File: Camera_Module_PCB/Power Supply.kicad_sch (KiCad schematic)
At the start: 18 parts

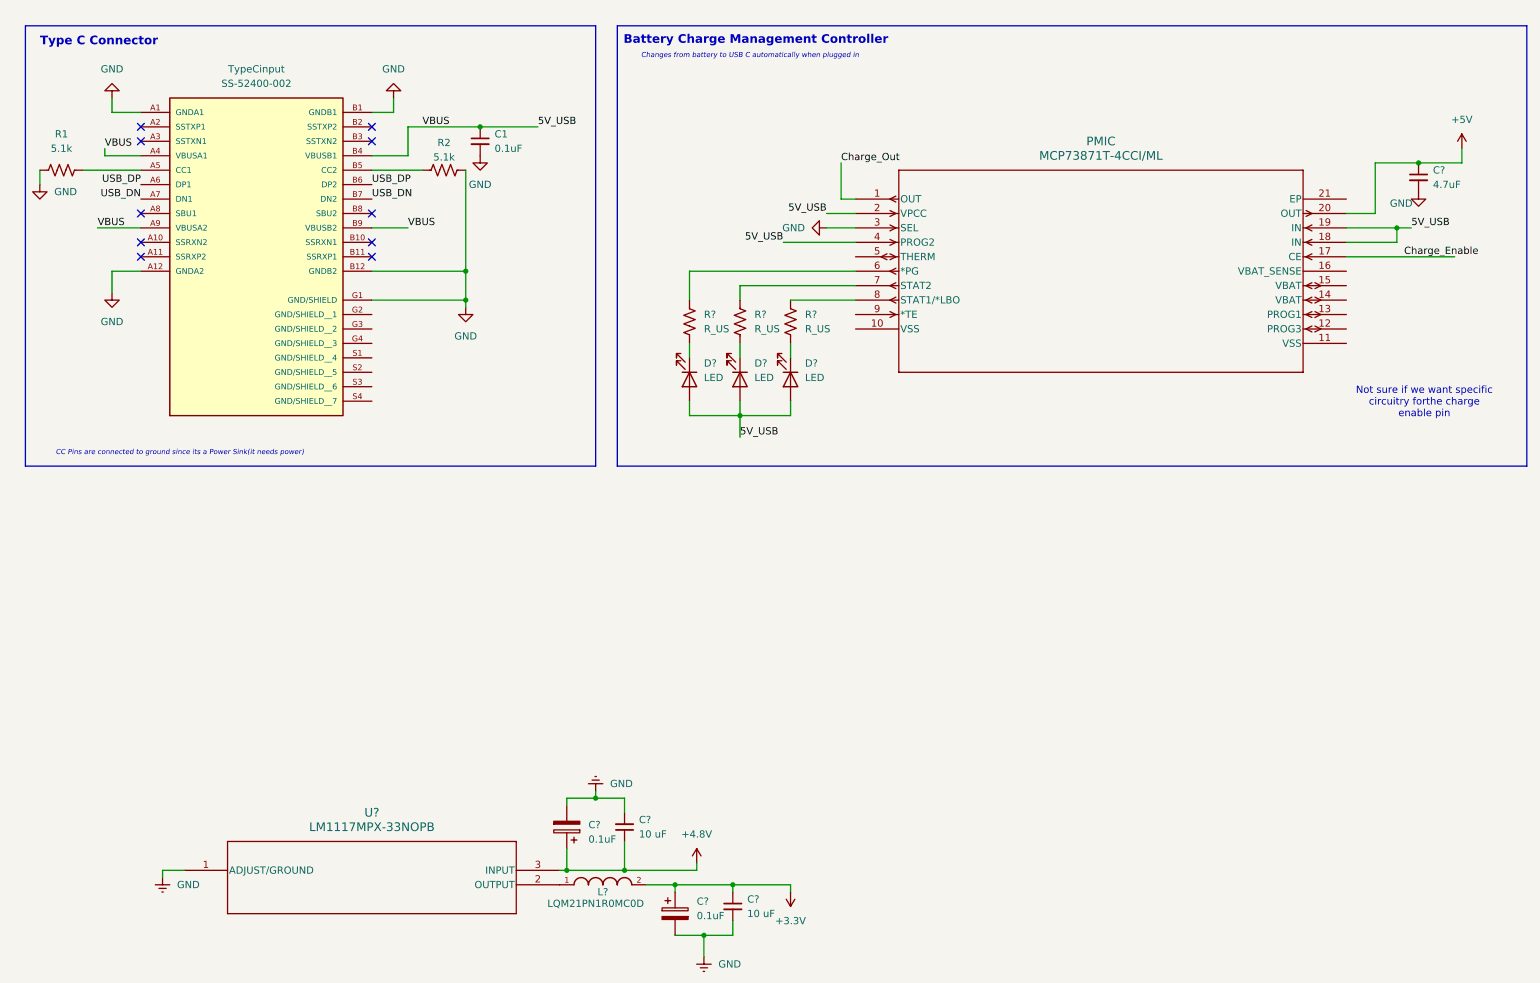
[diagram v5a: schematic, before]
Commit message: Small Additions to Charger
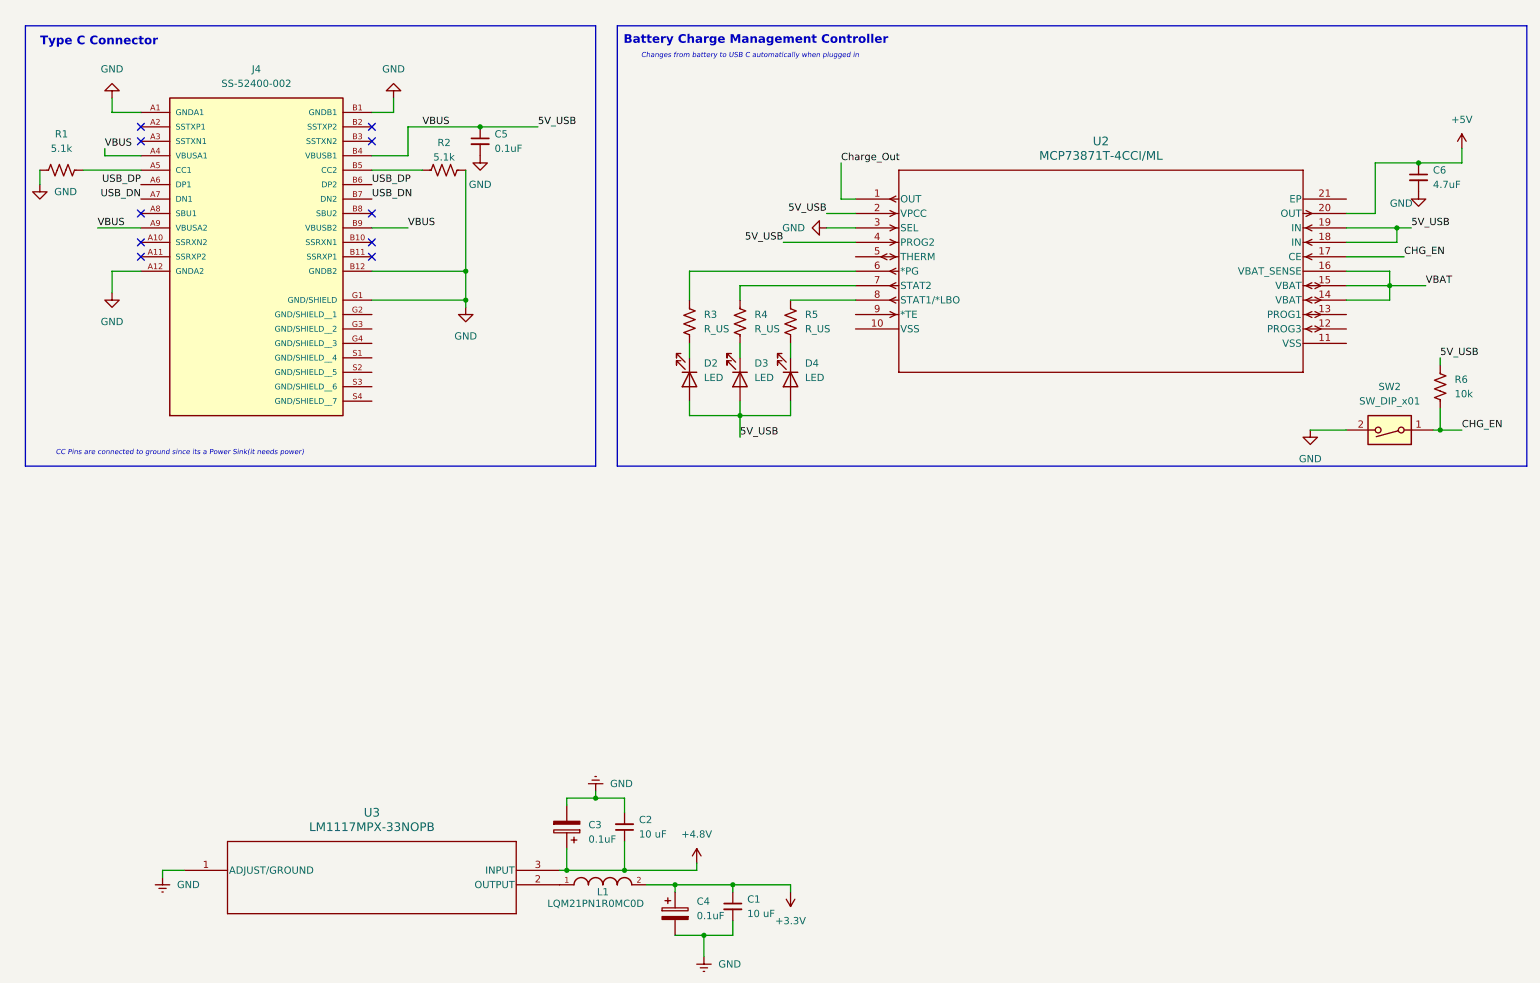
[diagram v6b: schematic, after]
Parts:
- added R6: 10k, symbol Device:R_US
- added SW2: SW_DIP_x01, symbol Switch:SW_DIP_x01
- gave numbers to parts that had none: 13
- renumbered C1 to C5, TypeCinput to J4, PMIC to U2
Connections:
- net 5V_USB: now also R6.1
- net GND: now also SW2.2
- net VBAT: now reaches U2.14 (VBAT)
- net VBAT: now also U2.15 (VBAT), U2.16 (VBAT_SENSE)
- net Charge_Enable renamed CHG_EN
- net CHG_EN: now also R6.2, SW2.1
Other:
- note removed: "Not sure if we want specific circuitry forthe charge enable pin"

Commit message: Made more small changes to the schematic
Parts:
- removed C3, C4: 0.1uF, symbol Device:C_Polarized
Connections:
- net +5V is gone; now on net V_OUT: C6.1, U2.20 (OUT)
- net +4.8V renamed V_OUT
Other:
- moved on the sheet: C1, C2

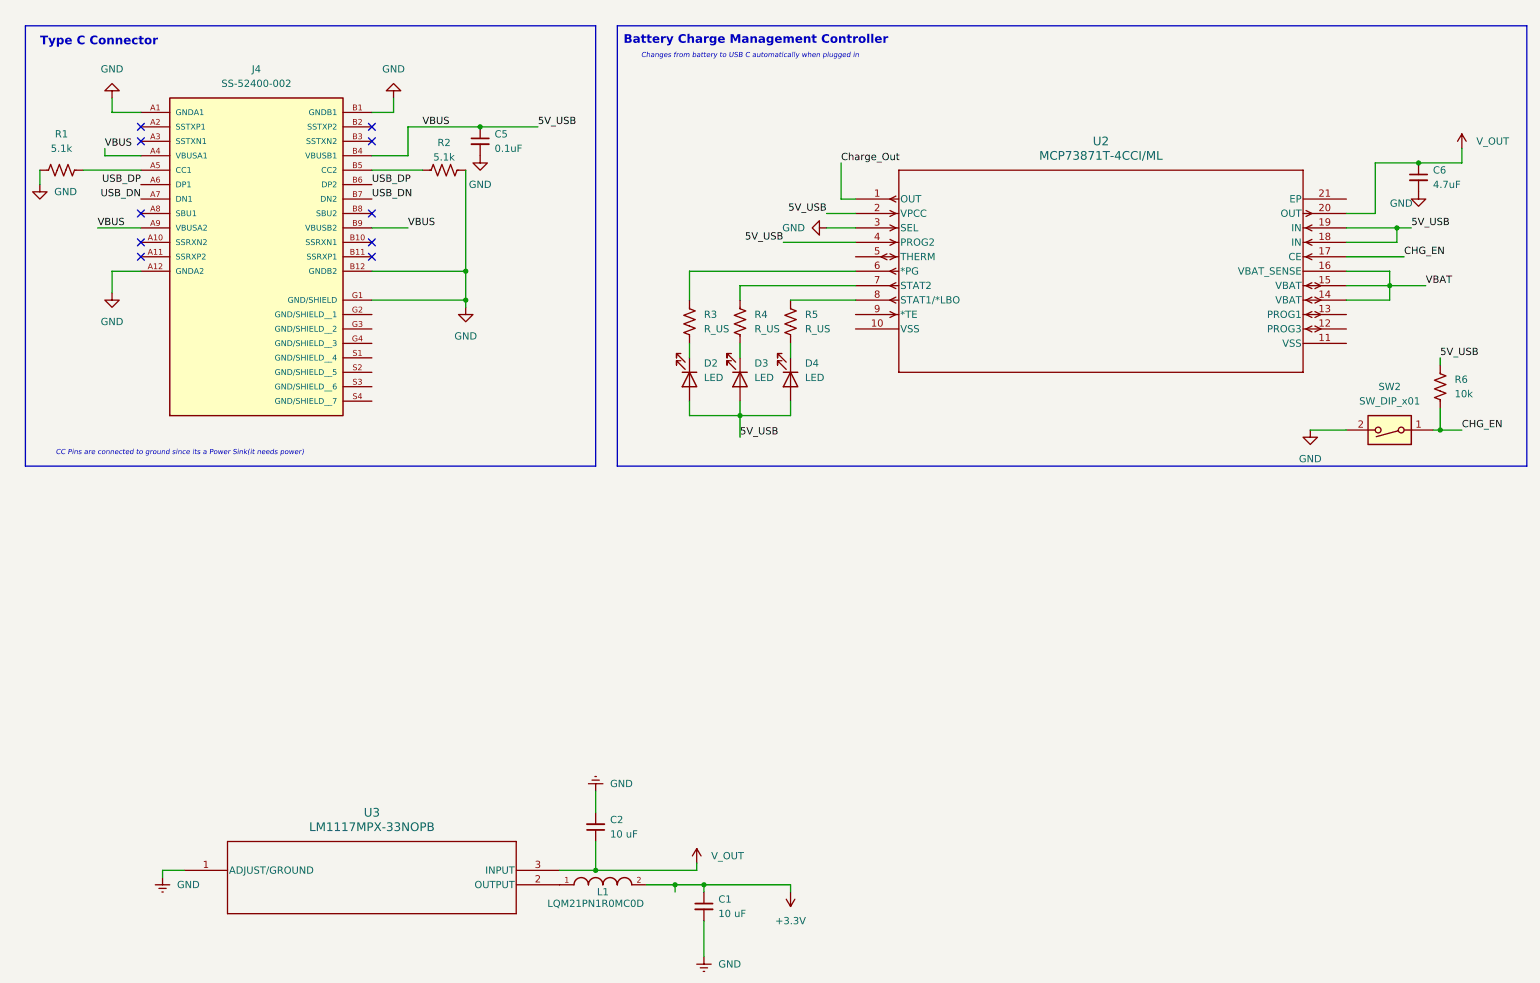
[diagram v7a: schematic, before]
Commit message: Update Power Supply.kicad_sch
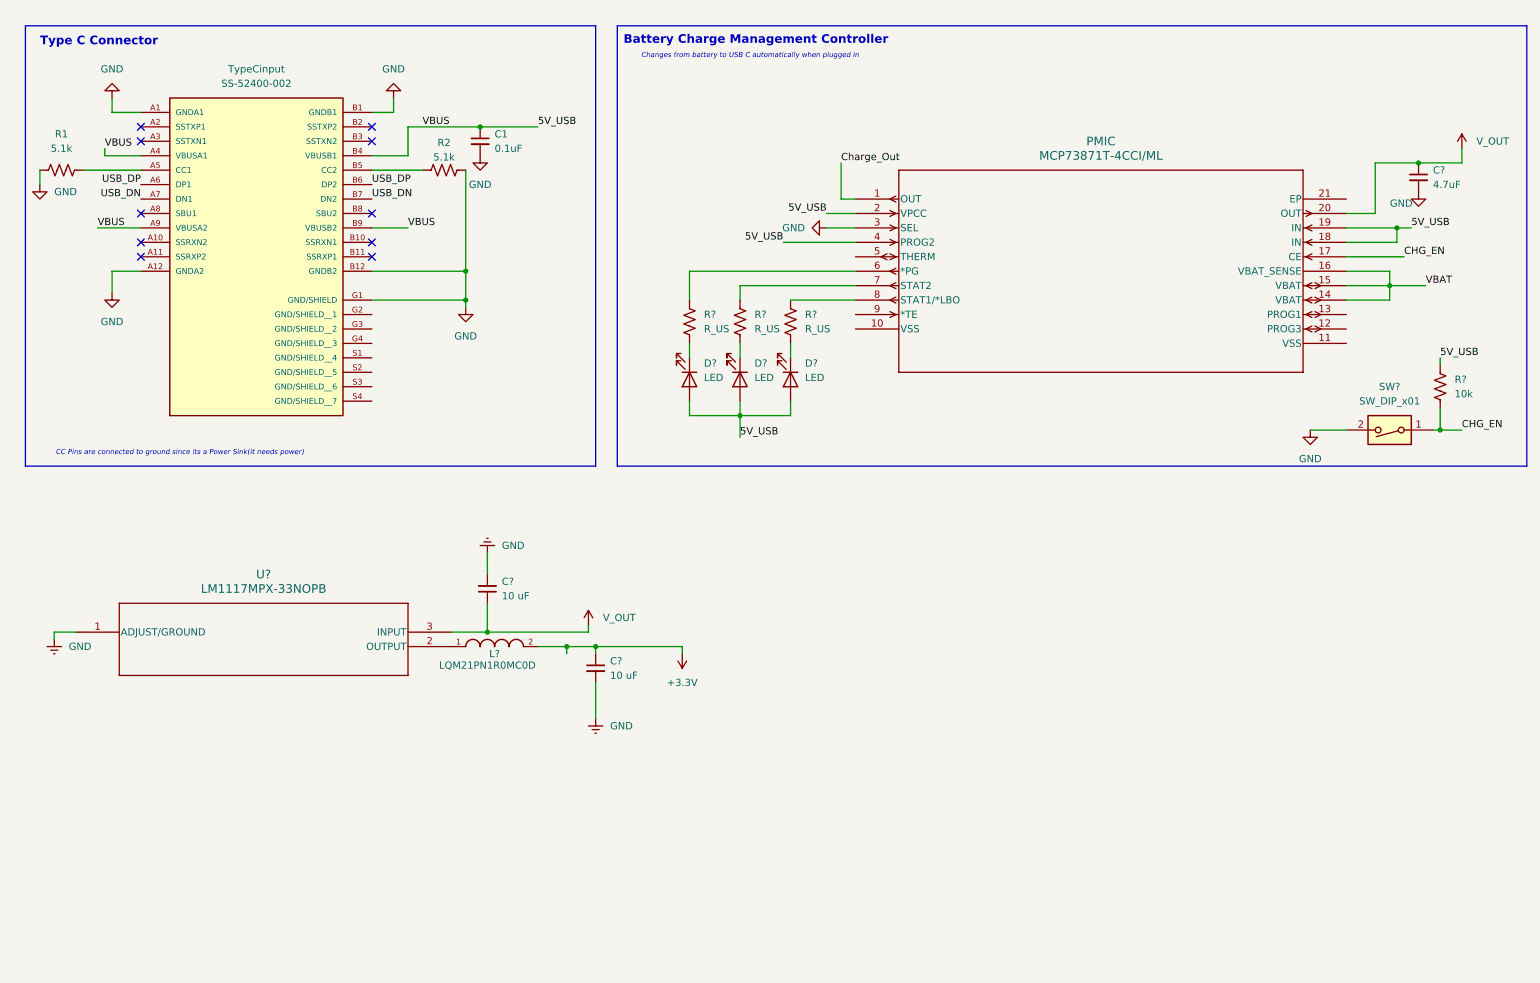
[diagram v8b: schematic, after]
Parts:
- renumbered C5 to C1, C6 to C?, C1 to C?, C2 to C?, D4 to D?, D2 to D?, D3 to D?, L1 to L?, U2 to PMIC, R3 to R?, R4 to R?, R6 to R?, R5 to R?, SW2 to SW?, J4 to TypeCinput, U3 to U?
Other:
- moved on the sheet: C?, L?, U?
